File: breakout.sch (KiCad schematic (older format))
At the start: 32 parts, among them CON1 SD_Card, CON2 USB-MICRO-AB, P2 CONN_01X40, P3 CONN_01X40, P4 CONN_01X40, P5 A-DF-09-A/KG-T4S, Q1 SIA461DJ-T1-GE3, SW1 SW_PUSH

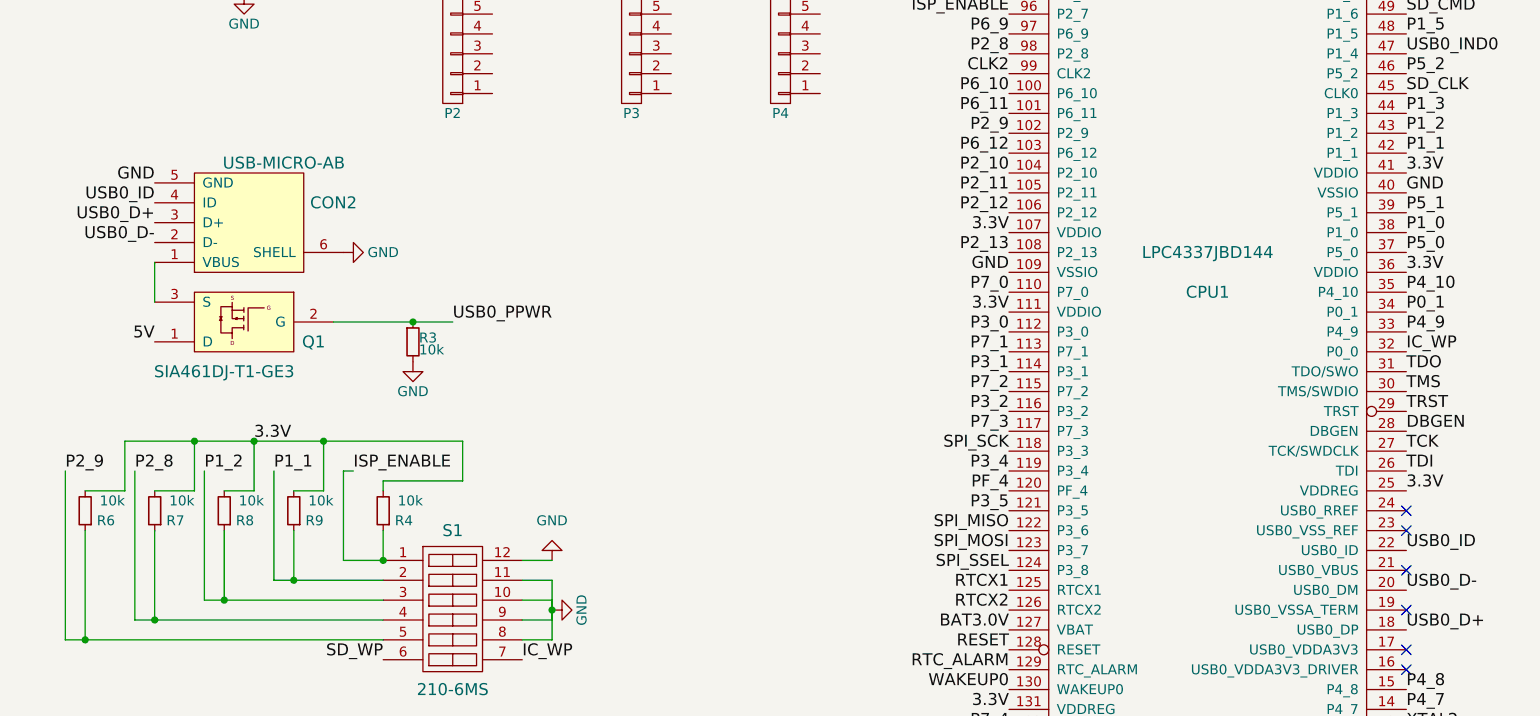
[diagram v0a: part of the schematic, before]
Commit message: added USB FET to schematic and board
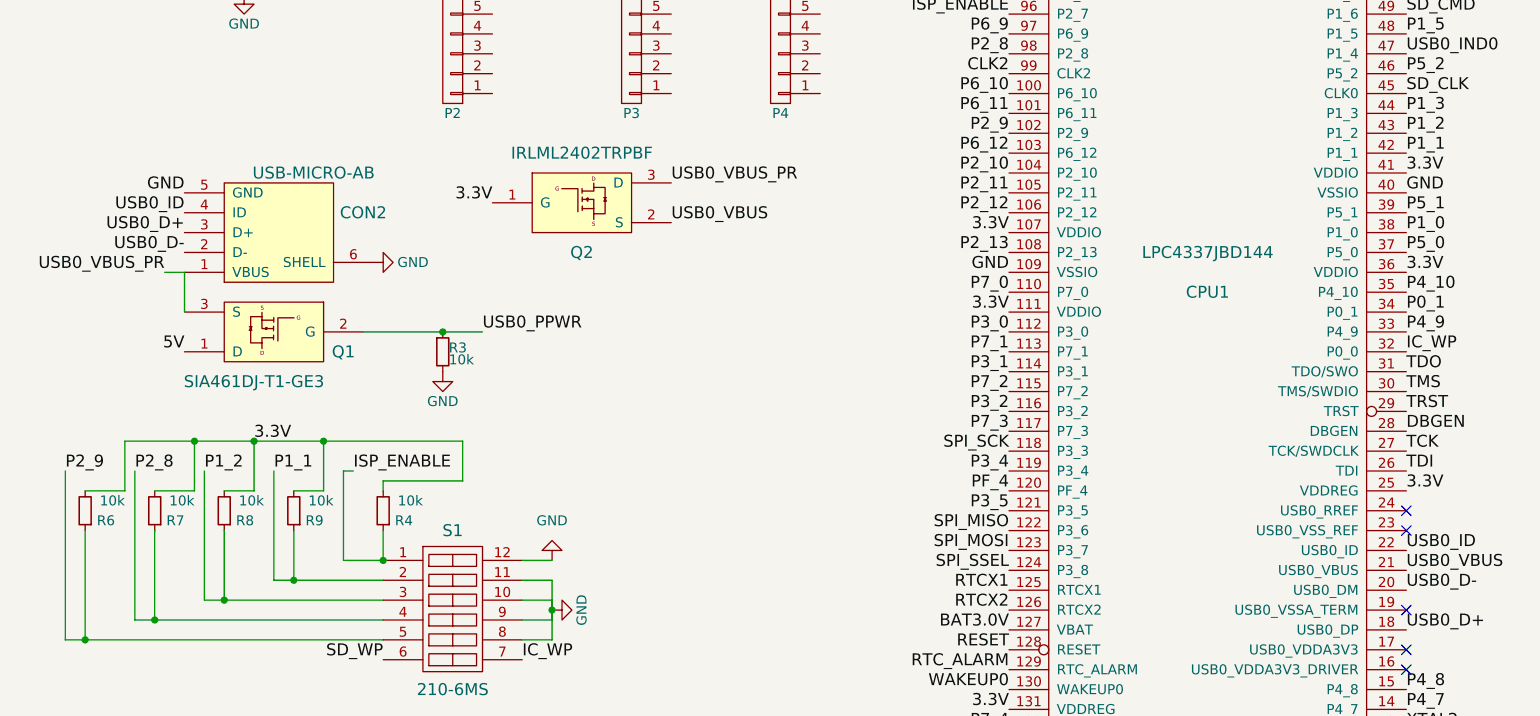
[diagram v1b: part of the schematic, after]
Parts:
- added Q2: IRLML2402TRPBF, Housings_SOT-23_SOT-143_TSOT-6:SOT-23, symbol IRLML2402TRPBF
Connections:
- net 3.3V: now also Q2.1 (G)
- net USB0_VBUS: now reaches CPU1.21 (USB0_VBUS)
- net USB0_VBUS: now also Q2.2 (S)
- net USB0_VBUS_PR: now reaches CON2.1 (VBUS), Q1.3 (S)
- net USB0_VBUS_PR: now also Q2.3 (D)
- no-connect marks 15 -> 14
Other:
- moved on the sheet: CON2, Q1, R3
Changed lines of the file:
@@
 LIBS:mpd
 LIBS:vishaysiliconix
+LIBS:infineon
 LIBS:breakout-cache
 EELAYER 25 0
@@
 $EndComp
 $Comp
-L PWR_FLAG #FLG1
+L PWR_FLAG #FLG01
 U 1 1 561BDFAD
 P 850 950
-F 0 "#FLG1" H 850 1045 50  0001 C CNN
+F 0 "#FLG01" H 850 1045 50  0001 C CNN
 F 1 "PWR_FLAG" V 1000 1100 50  0000 C CNN
 F 2 "" H 850 950 60  0000 C CNN
@@
 RAIL
 $Comp
-L GND #PWR1
+L GND #PWR02
 U 1 1 561BE928
 P 800 600
-F 0 "#PWR1" H 800 350 50  0001 C CNN
+F 0 "#PWR02" H 800 350 50  0001 C CNN
 F 1 "GND" V 800 400 50  0000 C CNN
 F 2 "" H 800 600 60  0000 C CNN
@@
 $EndComp
 $Comp
-L GND #PWR6
+L GND #PWR03
 U 1 1 561C5C16
 P 1600 2000
-F 0 "#PWR6" H 1600 1750 50  0001 C CNN
+F 0 "#PWR03" H 1600 1750 50  0001 C CNN
 F 1 "GND" H 1600 1850 50  0000 C CNN
 F 2 "" H 1600 2000 60  0000 C CNN
@@
 $EndComp
 $Comp
-L GND #PWR3
+L GND #PWR04
 U 1 1 561C5DB0
 P 1100 2550
-F 0 "#PWR3" H 1100 2300 50  0001 C CNN
+F 0 "#PWR04" H 1100 2300 50  0001 C CNN
 F 1 "GND" H 1100 2400 50  0000 C CNN
 F 2 "" H 1100 2550 60  0000 C CNN
@@
 $EndComp
 $Comp
-L GND #PWR8
+L GND #PWR05
 U 1 1 561C5E4C
 P 1900 2000
-F 0 "#PWR8" H 1900 1750 50  0001 C CNN
+F 0 "#PWR05" H 1900 1750 50  0001 C CNN
 F 1 "GND" H 1900 1850 50  0000 C CNN
 F 2 "" H 1900 2000 60  0000 C CNN
@@
 $EndComp
 $Comp
-L GND #PWR4
+L GND #PWR06
 U 1 1 561C689A
 P 1450 2550
-F 0 "#PWR4" H 1450 2300 50  0001 C CNN
+F 0 "#PWR06" H 1450 2300 50  0001 C CNN
 F 1 "GND" H 1450 2400 50  0000 C CNN
 F 2 "" H 1450 2550 60  0000 C CNN
@@
 $EndComp
 $Comp
-L GND #PWR9
+L GND #PWR07
 U 1 1 561C6F20
 P 2000 2550
-F 0 "#PWR9" H 2000 2300 50  0001 C CNN
+F 0 "#PWR07" H 2000 2300 50  0001 C CNN
 F 1 "GND" H 2000 2400 50  0000 C CNN
 F 2 "" H 2000 2550 60  0000 C CNN
@@
 $EndComp
 $Comp
-L GND #PWR13
+L GND #PWR08
 U 1 1 561ED8AD
 P 3050 9850
-F 0 "#PWR13" H 3050 9600 50  0001 C CNN
+F 0 "#PWR08" H 3050 9600 50  0001 C CNN
 F 1 "GND" H 3050 9700 50  0000 C CNN
 F 2 "" H 3050 9850 60  0000 C CNN
@@
 $EndComp
 $Comp
-L GND #PWR17
+L GND #PWR09
 U 1 1 561ED8D4
 P 3350 9450
-F 0 "#PWR17" H 3350 9200 50  0001 C CNN
+F 0 "#PWR09" H 3350 9200 50  0001 C CNN
 F 1 "GND" H 3350 9300 50  0000 C CNN
 F 2 "" H 3350 9450 60  0000 C CNN
@@
 $EndComp
 $Comp
-L GND #PWR2
+L GND #PWR010
 U 1 1 561F5842
 P 850 10250
-F 0 "#PWR2" H 850 10000 50  0001 C CNN
+F 0 "#PWR010" H 850 10000 50  0001 C CNN
 F 1 "GND" H 850 10100 50  0000 C CNN
 F 2 "" H 850 10250 60  0000 C CNN
@@
 L USB-MICRO-AB CON2
 U 1 1 561FF096
-P 1600 5250
-F 0 "CON2" H 2050 5150 60  0000 C CNN
-F 1 "USB-MICRO-AB" H 1800 4950 60  0000 C CNN
-F 2 "Custom Footprints:USB_MICRO_AB" H 1600 5250 60  0001 C CNN
-F 3 "" H 1600 5250 60  0000 C CNN
-	1    1600 5250
+P 1750 5300
+F 0 "CON2" H 2200 5200 60  0000 C CNN
+F 1 "USB-MICRO-AB" H 1950 5000 60  0000 C CNN
+F 2 "Custom Footprints:USB_MICRO_AB" H 1750 5300 60  0001 C CNN
+F 3 "" H 1750 5300 60  0000 C CNN
+	1    1750 5300
 	1    0    0    1
 $EndComp
-Text Label 1150 5050 2    60   ~ 0
+Text Label 1300 5100 2    60   ~ 0
 GND
 Text Label 7450 4400 0    60   ~ 0
 USB0_IND0
-NoConn ~ 7450 7000
-Text Label 1150 5850 2    60   ~ 0
+Text Label 1300 5900 2    60   ~ 0
 5V
-Text Label 2650 5750 0    60   ~ 0
+Text Label 2800 5800 0    60   ~ 0
 USB0_PPWR
 $Comp
 L R_Small R3
 U 1 1 56208A5C
-P 2450 5850
-F 0 "R3" H 2480 5870 50  0000 L CNN
-F 1 "10k" H 2480 5810 50  0000 L CNN
-F 2 "Resistors_SMD:R_0402" H 2450 5850 60  0001 C CNN
-F 3 "" H 2450 5850 60  0000 C CNN
-	1    2450 5850
-	1    0    0    -1
-$EndComp
-$Comp
-L GND #PWR11
+P 2600 5900
+F 0 "R3" H 2630 5920 50  0000 L CNN
+F 1 "10k" H 2630 5860 50  0000 L CNN
+F 2 "Resistors_SMD:R_0402" H 2600 5900 60  0001 C CNN
+F 3 "" H 2600 5900 60  0000 C CNN
+	1    2600 5900
+	1    0    0    -1
+$EndComp
+$Comp
+L GND #PWR011
 U 1 1 56208A99
-P 2450 5950
-F 0 "#PWR11" H 2450 5700 50  0001 C CNN
-F 1 "GND" H 2450 5800 50  0000 C CNN
-F 2 "" H 2450 5950 60  0000 C CNN
-F 3 "" H 2450 5950 60  0000 C CNN
-	1    2450 5950
+P 2600 6000
+F 0 "#PWR011" H 2600 5750 50  0001 C CNN
+F 1 "GND" H 2600 5850 50  0000 C CNN
+F 2 "" H 2600 6000 60  0000 C CNN
+F 3 "" H 2600 6000 60  0000 C CNN
+	1    2600 6000
 	1    0    0    -1
 $EndComp
@@
 $EndComp
 $Comp
-L GND #PWR15
+L GND #PWR012
 U 1 1 56282950
 P 3150 6950
-F 0 "#PWR15" H 3150 6700 50  0001 C CNN
+F 0 "#PWR012" H 3150 6700 50  0001 C CNN
 F 1 "GND" H 3150 6750 50  0000 C CNN
 F 2 "" H 3150 6950 60  0000 C CNN
@@
 $EndComp
 $Comp
-L GND #PWR5
+L GND #PWR013
 U 1 1 562864C0
 P 1550 8250
-F 0 "#PWR5" H 1550 8000 50  0001 C CNN
+F 0 "#PWR013" H 1550 8000 50  0001 C CNN
 F 1 "GND" H 1550 8100 50  0000 C CNN
 F 2 "" H 1550 8250 60  0000 C CNN
@@
 GND
 $Comp
-L GND #PWR16
+L GND #PWR014
 U 1 1 562880B7
 P 3150 7200
-F 0 "#PWR16" H 3150 6950 50  0001 C CNN
+F 0 "#PWR014" H 3150 6950 50  0001 C CNN
 F 1 "GND" H 3150 7050 50  0000 C CNN
 F 2 "" H 3150 7200 60  0000 C CNN
@@
 BAT3.0V
 $Comp
-L GND #PWR7
+L GND #PWR015
 U 1 1 563D5013
 P 1600 4100
-F 0 "#PWR7" H 1600 3850 50  0001 C CNN
+F 0 "#PWR015" H 1600 3850 50  0001 C CNN
 F 1 "GND" H 1600 3950 50  0000 C CNN
 F 2 "" H 1600 4100 60  0000 C CNN
@@
 	1    0    0    -1
 $EndComp
-Text Label 1150 5150 2    60   ~ 0
+Text Label 1300 5200 2    60   ~ 0
 USB0_ID
 Text Label 7450 6900 0    60   ~ 0
 USB0_ID
-Text Label 1150 5250 2    60   ~ 0
+Text Label 1300 5300 2    60   ~ 0
 USB0_D+
-Text Label 1150 5350 2    60   ~ 0
+Text Label 1300 5400 2    60   ~ 0
 USB0_D-
 Text Label 7450 7100 0    60   ~ 0
@@
 Connection ~ 2350 9650
 Wire Wire Line
-	1150 5650 1150 5450
-Wire Wire Line
-	2050 5750 2650 5750
-Connection ~ 2450 5750
+	1300 5700 1300 5500
+Wire Wire Line
+	2200 5800 2800 5800
+Connection ~ 2600 5800
 Wire Wire Line
 	5050 1050 6100 1050
@@
 	1850 6600 2000 6600
 Wire Wire Line
-	2000 6350 2000 6600
+	2000 6600 2000 6350
 Wire Wire Line
 	1000 6350 2700 6350
@@
 P1_0
 $Comp
-L GND #PWR12
+L GND #PWR016
 U 1 1 565E50DA
 P 2600 8550
-F 0 "#PWR12" H 2600 8300 50  0001 C CNN
+F 0 "#PWR016" H 2600 8300 50  0001 C CNN
 F 1 "GND" V 2600 8350 50  0000 C CNN
 F 2 "" H 2600 8550 60  0000 C CNN
@@
 $EndComp
 $Comp
-L GND #PWR10
+L GND #PWR017
 U 1 1 565E5A43
-P 2100 5400
-F 0 "#PWR10" H 2100 5150 50  0001 C CNN
-F 1 "GND" V 2100 5200 50  0000 C CNN
-F 2 "" H 2100 5400 60  0000 C CNN
-F 3 "" H 2100 5400 60  0000 C CNN
-	1    2100 5400
+P 2250 5450
+F 0 "#PWR017" H 2250 5200 50  0001 C CNN
+F 1 "GND" V 2250 5250 50  0000 C CNN
+F 2 "" H 2250 5450 60  0000 C CNN
+F 3 "" H 2250 5450 60  0000 C CNN
+	1    2250 5450
 	0    -1   -1   0
 $EndComp
@@
 	5050 2700 5450 2700
 $Comp
-L GND #PWR14
+L GND #PWR018
 U 1 1 566387B9
 P 3100 2150
-F 0 "#PWR14" H 3100 1900 50  0001 C CNN
+F 0 "#PWR018" H 3100 1900 50  0001 C CNN
 F 1 "GND" H 3100 2000 50  0000 C CNN
 F 2 "" H 3100 2150 60  0000 C CNN
@@
 L SIA461DJ-T1-GE3 Q1
 U 1 1 5664957E
-P 1600 5750
-F 0 "Q1" H 1250 5650 60  0000 C CNN
-F 1 "SIA461DJ-T1-GE3" H 1700 5500 60  0000 C CNN
-F 2 "Custom Footprints:PowerPak_SC-70-6L-Single" H 1600 5750 60  0001 C CNN
-F 3 "" H 1600 5750 60  0000 C CNN
-	1    1600 5750
+P 1750 5800
+F 0 "Q1" H 1400 5700 60  0000 C CNN
+F 1 "SIA461DJ-T1-GE3" H 1850 5550 60  0000 C CNN
+F 2 "Custom Footprints:PowerPak_SC-70-6L-Single" H 1750 5800 60  0001 C CNN
+F 3 "" H 1750 5800 60  0000 C CNN
+	1    1750 5800
 	-1   0    0    -1
 $EndComp
+Wire Wire Line
+	1300 5500 1200 5500
+Text Label 1200 5500 2    60   ~ 0
+USB0_VBUS_PR
+Text Label 3750 5050 0    60   ~ 0
+USB0_VBUS_PR
+$Comp
+L IRLML2402TRPBF Q2
+U 1 1 566407D6
+P 3300 5150
+F 0 "Q2" H 3300 4900 60  0000 C CNN
+F 1 "IRLML2402TRPBF" H 3300 5400 60  0000 C CNN
+F 2 "Housings_SOT-23_SOT-143_TSOT-6:SOT-23" H 3300 5150 60  0001 C CNN
+F 3 "" H 3300 5150 60  0000 C CNN
+	1    3300 5150
+	1    0    0    -1
+$EndComp
+Text Label 2850 5150 2    60   ~ 0
+3.3V
+Text Label 7450 7000 0    60   ~ 0
+USB0_VBUS
+Text Label 3750 5250 0    60   ~ 0
+USB0_VBUS
 $EndSCHEMATC

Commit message: added USB0_RREF and 12K resistor
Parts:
- added R1: 12K, Resistors_SMD:R_0603, symbol R_Small
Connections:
- net GND: now also R1.2
- net USB0_RREF: now reaches CPU1.24 (USB0_RREF)
- net USB0_RREF: now also R1.1
- no-connect marks 14 -> 13
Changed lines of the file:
@@
 NoConn ~ 7450 7200
 NoConn ~ 7450 6800
-NoConn ~ 7450 6700
 Text Label 7450 6400 0    60   ~ 0
 TCK
@@
 Text Label 3750 5250 0    60   ~ 0
 USB0_VBUS
+Text Label 800  4700 0    60   ~ 0
+USB0_RREF
+$Comp
+L R_Small R1
+U 1 1 56644916
+P 800 4800
+F 0 "R1" H 830 4820 50  0000 L CNN
+F 1 "12K" H 830 4760 50  0000 L CNN
+F 2 "Resistors_SMD:R_0603" H 800 4800 60  0001 C CNN
+F 3 "" H 800 4800 60  0000 C CNN
+	1    800  4800
+	1    0    0    -1
+$EndComp
+$Comp
+L GND #PWR019
+U 1 1 56644987
+P 800 4900
+F 0 "#PWR019" H 800 4650 50  0001 C CNN
+F 1 "GND" H 800 4750 50  0000 C CNN
+F 2 "" H 800 4900 60  0000 C CNN
+F 3 "" H 800 4900 60  0000 C CNN
+	1    800  4900
+	1    0    0    -1
+$EndComp
+Text Label 7450 6700 0    60   ~ 0
+USB0_RREF
 $EndSCHEMATC

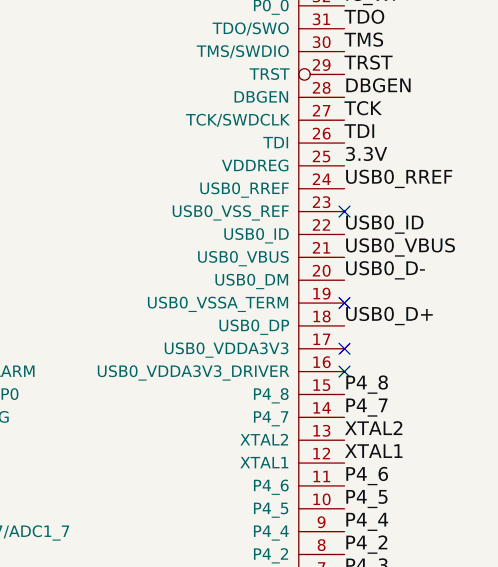
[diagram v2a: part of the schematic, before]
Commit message: added the NC'd USB0 pins, and fixed some trace sizes
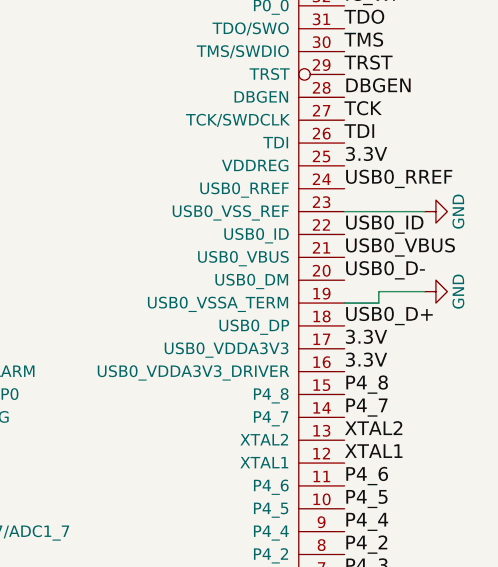
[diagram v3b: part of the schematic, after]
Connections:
- net 3.3V: now also CPU1.16 (USB0_VDDA3V3_DRIVER), CPU1.17 (USB0_VDDA3V3)
- net GND: now also CPU1.19 (USB0_VSSA_TERM), CPU1.23 (USB0_VSS_REF)
- no-connect marks 13 -> 9
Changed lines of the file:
@@
 Text Label 7450 7600 0    60   ~ 0
 P4_8
-NoConn ~ 7450 7500
-NoConn ~ 7450 7400
-NoConn ~ 7450 7200
-NoConn ~ 7450 6800
 Text Label 7450 6400 0    60   ~ 0
 TCK
@@
 Text Label 7450 6700 0    60   ~ 0
 USB0_RREF
+Text Label 7450 7400 0    60   ~ 0
+3.3V
+Text Label 7450 7500 0    60   ~ 0
+3.3V
+$Comp
+L GND #PWR020
+U 1 1 566486A9
+P 7800 6800
+F 0 "#PWR020" H 7800 6550 50  0001 C CNN
+F 1 "GND" H 7800 6650 50  0000 C CNN
+F 2 "" H 7800 6800 60  0000 C CNN
+F 3 "" H 7800 6800 60  0000 C CNN
+	1    7800 6800
+	0    -1   -1   0
+$EndComp
+Wire Wire Line
+	7800 6800 7450 6800
+$Comp
+L GND #PWR021
+U 1 1 5664879C
+P 7800 7150
+F 0 "#PWR021" H 7800 6900 50  0001 C CNN
+F 1 "GND" H 7800 7000 50  0000 C CNN
+F 2 "" H 7800 7150 60  0000 C CNN
+F 3 "" H 7800 7150 60  0000 C CNN
+	1    7800 7150
+	0    -1   -1   0
+$EndComp
+Wire Wire Line
+	7800 7150 7600 7150
+Wire Wire Line
+	7600 7150 7600 7200
+Wire Wire Line
+	7600 7200 7450 7200
 $EndSCHEMATC

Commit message: added test points
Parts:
- added W2, W3: TEST, Measurement_Points:Measurement_Point_Round-SMD-Pad_Small, symbol TEST
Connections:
- net 3.3V: no longer R4.2, R6.2, R7.2, R8.2, R9.2
- net USB0_PPWR: now also W2.1
- net USB0_VBUS: now also W3.1
- no-connect marks 9 -> 11
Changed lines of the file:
@@
 	-1   0    0    1
 $EndComp
-Text Label 1650 6350 0    60   ~ 0
+Text Label 850  6350 2    60   ~ 0
 3.3V
 Text Label 5450 4800 2    60   ~ 0
@@
 	1850 6600 2000 6600
 Wire Wire Line
-	2000 6600 2000 6350
-Wire Wire Line
-	1000 6350 2700 6350
-Wire Wire Line
-	2700 6350 2700 6550
+	2000 6600 2000 6450
+Wire Wire Line
+	2700 6450 2700 6550
 Wire Wire Line
 	2700 6550 2300 6550
 Wire Wire Line
 	2300 6550 2300 6600
-Connection ~ 2000 6350
 Wire Wire Line
 	1500 6600 1650 6600
 Wire Wire Line
-	1650 6600 1650 6350
+	1650 6600 1650 6450
 Wire Wire Line
 	1150 6600 1350 6600
 Wire Wire Line
-	1350 6600 1350 6350
-Connection ~ 1650 6350
+	1350 6600 1350 6450
 Wire Wire Line
 	800  6600 1000 6600
 Wire Wire Line
-	1000 6600 1000 6350
-Connection ~ 1350 6350
+	1000 6600 1000 6450
 Wire Wire Line
 	700  6500 700  7350
@@
 Wire Wire Line
 	7600 7200 7450 7200
+$Comp
+L TEST W3
+U 1 1 5664A7E2
+P 3750 5450
+F 0 "W3" H 3750 5510 40  0000 C CNN
+F 1 "TEST" H 3750 5380 40  0000 C CNN
+F 2 "Measurement_Points:Measurement_Point_Round-SMD-Pad_Small" H 3750 5450 60  0001 C CNN
+F 3 "" H 3750 5450 60  0000 C CNN
+	1    3750 5450
+	0    1    1    0
+$EndComp
+$Comp
+L TEST W2
+U 1 1 5664C3C0
+P 2350 6000
+F 0 "W2" H 2350 6060 40  0000 C CNN
+F 1 "TEST" H 2350 5930 40  0000 C CNN
+F 2 "Measurement_Points:Measurement_Point_Round-SMD-Pad_Small" H 2350 6000 60  0001 C CNN
+F 3 "" H 2350 6000 60  0000 C CNN
+	1    2350 6000
+	0    1    1    0
+$EndComp
+NoConn ~ 2350 6200
+NoConn ~ 3750 5650
+Entry Wire Line
+	1250 6350 1350 6450
+Entry Wire Line
+	1550 6350 1650 6450
+Entry Wire Line
+	1900 6350 2000 6450
+Entry Wire Line
+	2600 6350 2700 6450
+Entry Wire Line
+	900  6350 1000 6450
+Wire Bus Line
+	2600 6350 850  6350
+Connection ~ 2350 5800
 $EndSCHEMATC

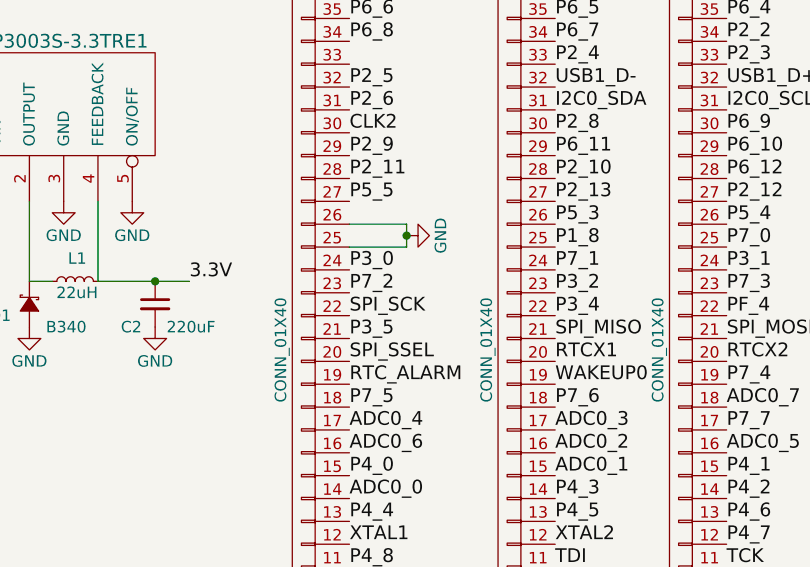
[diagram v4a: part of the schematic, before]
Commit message: connected RESET to a header pin
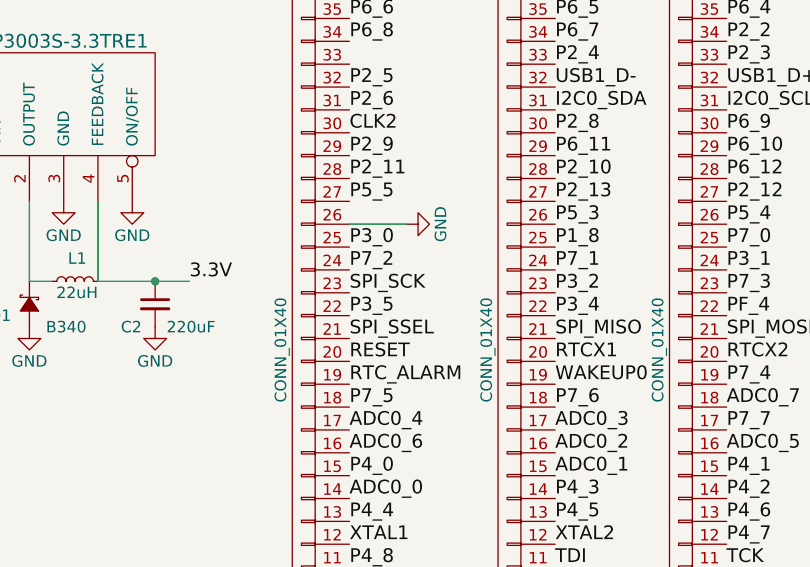
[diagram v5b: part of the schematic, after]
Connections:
- net GND: no longer P2.25 (P25)
- net P3_0: now also P2.25 (P25); no longer P2.24 (P24)
- net P3_5: now also P2.22 (P22); no longer P2.21 (P21)
- net P7_2: now also P2.24 (P24); no longer P2.23 (P23)
- net RESET: now also P2.20 (P20)
- net SPI_SCK: now also P2.23 (P23); no longer P2.22 (P22)
- net SPI_SSEL: now also P2.21 (P21); no longer P2.20 (P20)
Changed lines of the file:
@@
 Text Label 3750 2700 0    60   ~ 0
 RTCX1
-Text Label 2850 2600 0    60   ~ 0
+Text Label 2850 2500 0    60   ~ 0
 P3_5
 Text Label 4500 2500 0    60   ~ 0
 PF_4
-Text Label 2850 2700 0    60   ~ 0
+Text Label 2850 2600 0    60   ~ 0
 SPI_SSEL
 Text Label 4500 2600 0    60   ~ 0
@@
 Text Label 3750 2500 0    60   ~ 0
 P3_4
-Text Label 2850 2500 0    60   ~ 0
+Text Label 2850 2400 0    60   ~ 0
 SPI_SCK
 Text Label 4500 2400 0    60   ~ 0
@@
 Text Label 3750 2400 0    60   ~ 0
 P3_2
-Text Label 2850 2400 0    60   ~ 0
+Text Label 2850 2300 0    60   ~ 0
 P7_2
 Text Label 4500 2300 0    60   ~ 0
@@
 Text Label 3750 2300 0    60   ~ 0
 P7_1
-Text Label 2850 2300 0    60   ~ 0
+Text Label 2850 2200 0    60   ~ 0
 P3_0
 Text Label 4500 2200 0    60   ~ 0
@@
 L GND #PWR018
 U 1 1 566387B9
-P 3100 2150
-F 0 "#PWR018" H 3100 1900 50  0001 C CNN
-F 1 "GND" H 3100 2000 50  0000 C CNN
-F 2 "" H 3100 2150 60  0000 C CNN
-F 3 "" H 3100 2150 60  0000 C CNN
-	1    3100 2150
+P 3100 2100
+F 0 "#PWR018" H 3100 1850 50  0001 C CNN
+F 1 "GND" H 3100 1950 50  0000 C CNN
+F 2 "" H 3100 2100 60  0000 C CNN
+F 3 "" H 3100 2100 60  0000 C CNN
+	1    3100 2100
 	0    -1   -1   0
 $EndComp
 Wire Wire Line
 	2850 2100 3100 2100
-Wire Wire Line
-	3100 2100 3100 2200
-Wire Wire Line
-	3100 2200 2850 2200
-Connection ~ 3100 2150
 $Comp
 L SIA461DJ-T1-GE3 Q1
@@
 	2600 6350 850  6350
 Connection ~ 2350 5800
+Text Label 2850 2700 0    60   ~ 0
+RESET
 $EndSCHEMATC
